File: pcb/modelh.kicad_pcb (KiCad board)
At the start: 2 copper layers, 150 x 38 mm, 51 parts, among them J1 USB_B, J2 Conn_cols, J3 Conn_rows, J4 Conn_leds, J5 Conn_02x03_Odd_Even, J6 Conn_02x05_Odd_Even, J7 Conn_01x05, J8 Conn_01x05, J9 Conn_01x05, SW1 SW_Push, U1 STM32F103C8Tx, U2 AMS1117-3.3, Y1 8MHz

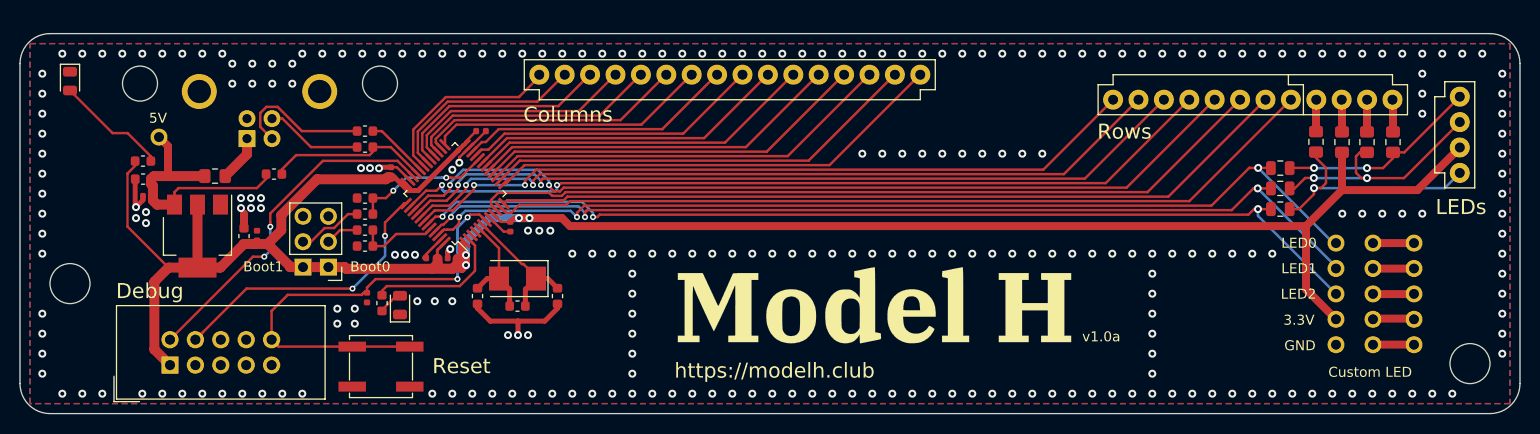
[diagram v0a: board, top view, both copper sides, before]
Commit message: Substitutes USB B connector with USB C connector
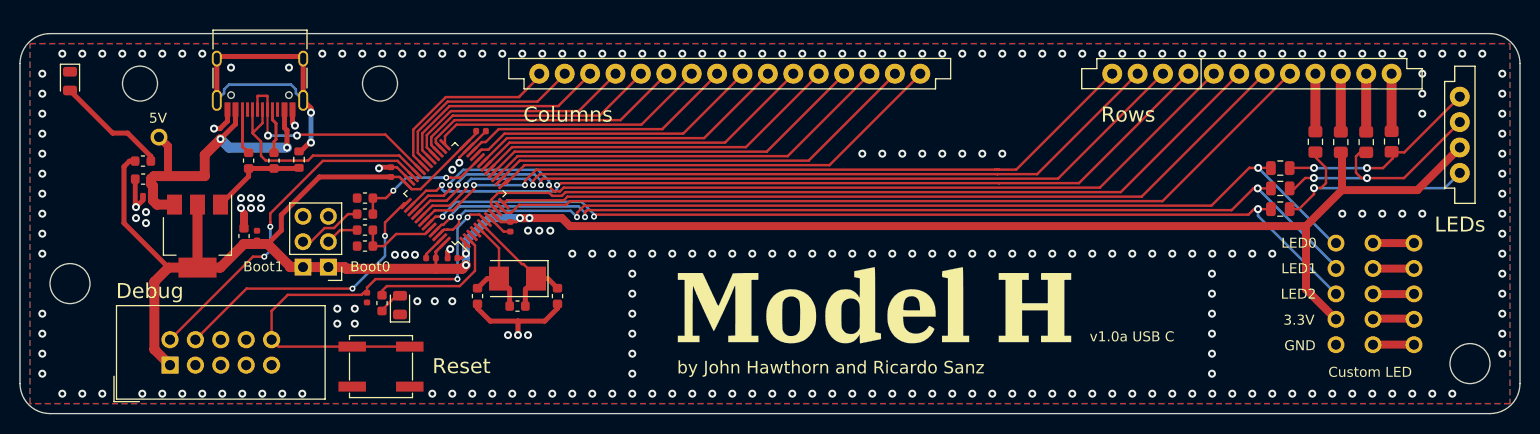
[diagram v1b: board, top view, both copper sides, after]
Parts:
- removed R16: 0, Resistor_SMD:R_0805_2012Metric_Pad1.15x1.40mm_HandSolder
- J1: value USB_B -> USB_C_Receptacle_USB2.0; footprint Connector_USB:USB_B_OST_USB-B1HSxx_Horizontal -> Connector_USB:USB_C_Receptacle_HRO_TYPE-C-31-M-12
- J2: value Conn_cols -> Conn_01x16
- J3: value Conn_rows -> Conn_01x12
- J4: value Conn_leds -> Conn_01x04
- R11: value 1.5k -> 1M
- moved R4 12.0 mm to (87.6, 59.7), turned to -90 degrees
- moved R3 9.20 mm to (90.2, 59.7), turned to -90 degrees
- moved J1 7.07 mm to (88.8, 50.5), turned to 180 degrees
- moved R11 2.89 mm to (92.7, 59.6), turned to 90 degrees
- moved J3 1.60 mm to (188.0, 51.0)
- moved R15 0.15 mm to (201.9, 57.8)
- moved R13 0.12 mm to (196.8, 57.8)
- moved J2 0.10 mm to (135.8, 51.0)
- moved R14 0.08 mm to (199.4, 57.8)
- moved R12 0.06 mm to (194.3, 57.8)
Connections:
- J6 pad 5: (no net) -> unconnected-(J6-Pad5)
- J6 pad 6: (no net) -> unconnected-(J6-Pad6)
- J6 pad 8: (no net) -> unconnected-(J6-Pad8)
- R11 pad 1: D+ -> GND
- R11 pad 2: +5V -> SHIELD
- R3 pad 1: Net-(J1-Pad3) -> CC1
- R3 pad 2: D+ -> GND
- R4 pad 1: Net-(J1-Pad2) -> CC2
- R4 pad 2: D- -> GND
- U1 pad 3: (no net) -> unconnected-(U1-Pad3)
- U1 pad 4: (no net) -> unconnected-(U1-Pad4)
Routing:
- net SHIELD: track 0.00 -> 33.9 mm, vias 0 -> 2
- net D-: track 6.33 -> 22.7 mm, vias 0 -> 2
- net GND: track 31.3 -> 45.4 mm, vias 268 -> 258
- net Net-(J1-Pad2): track 14.0 -> 0.00 mm
- net Net-(J1-Pad3): track 9.69 -> 0.00 mm
- net +3V3: track 229.5 -> 220.1 mm
- net D+: track 16.2 -> 25.1 mm
- net +5V: track 25.8 -> 33.9 mm, vias 0 -> 2
- net CC2: track 0.00 -> 4.92 mm
- net CC1: track 0.00 -> 4.90 mm
- net Net-(J1-Pad1): track 4.72 -> 0.00 mm
- net Net-(J3-Pad11): track 3.27 -> 5.81 mm
- net Net-(J3-Pad9): track 3.26 -> 5.79 mm
- net Net-(J3-Pad10): track 3.29 -> 5.81 mm
- net Net-(R15-Pad1): track 3.30 -> 5.76 mm
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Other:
- net class Default removed
- board text added: "by John Hawthorn and Ricardo Sanz"
- board text added: "v1.0a USB C"
- board text removed: "https://modelh.club"
- board text removed: "v1.0a"

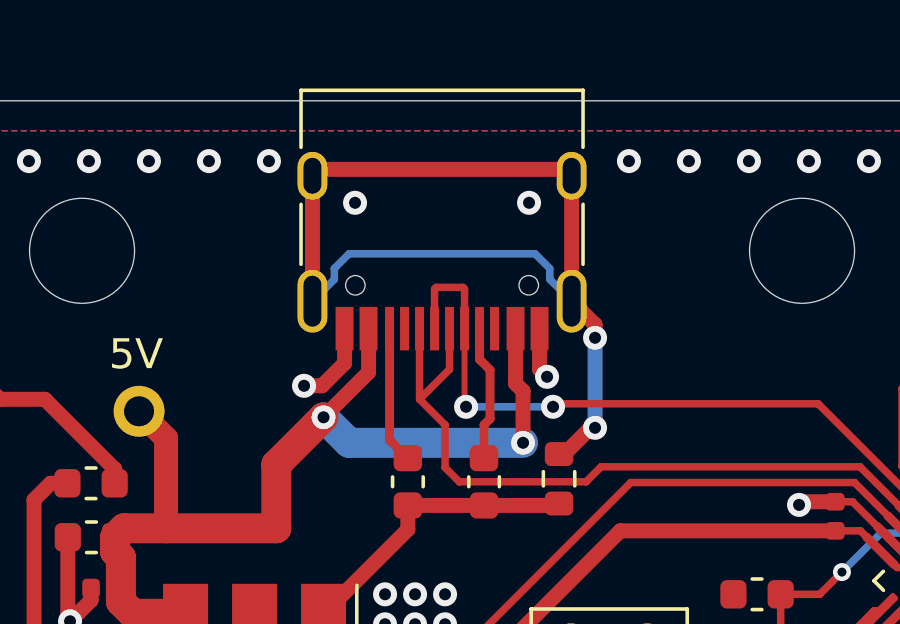
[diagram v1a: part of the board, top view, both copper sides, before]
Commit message: Updates 3D models and moves USB closer to edge
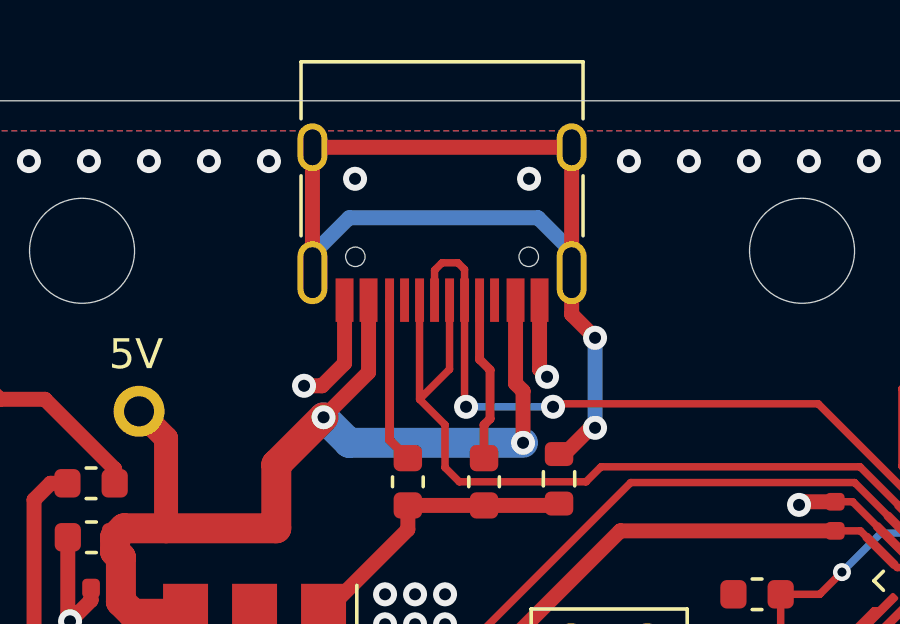
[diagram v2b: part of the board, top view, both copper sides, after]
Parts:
- moved J1 0.95 mm to (88.8, 49.6)
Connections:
- net CC1 renamed Net-(J1-PadA5)
- net CC2 renamed Net-(J1-PadB5)
- net SHIELD renamed Net-(J1-PadS1)
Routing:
- net GND: track 45.4 -> 47.3 mm
- net +5V: track 33.9 -> 35.1 mm
- net Net-(J1-PadS1): track 33.9 -> 35.0 mm
- net Net-(J1-PadB5): track 4.92 -> 5.52 mm
- net Net-(J1-PadA5): track 4.90 -> 5.50 mm
- net D+: track 25.1 -> 25.7 mm
